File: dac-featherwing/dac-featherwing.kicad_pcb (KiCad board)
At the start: 2 copper layers, 22.9 x 50.7 mm, 14 parts, among them J1 BOT, J2 TOP, U1 WM1824

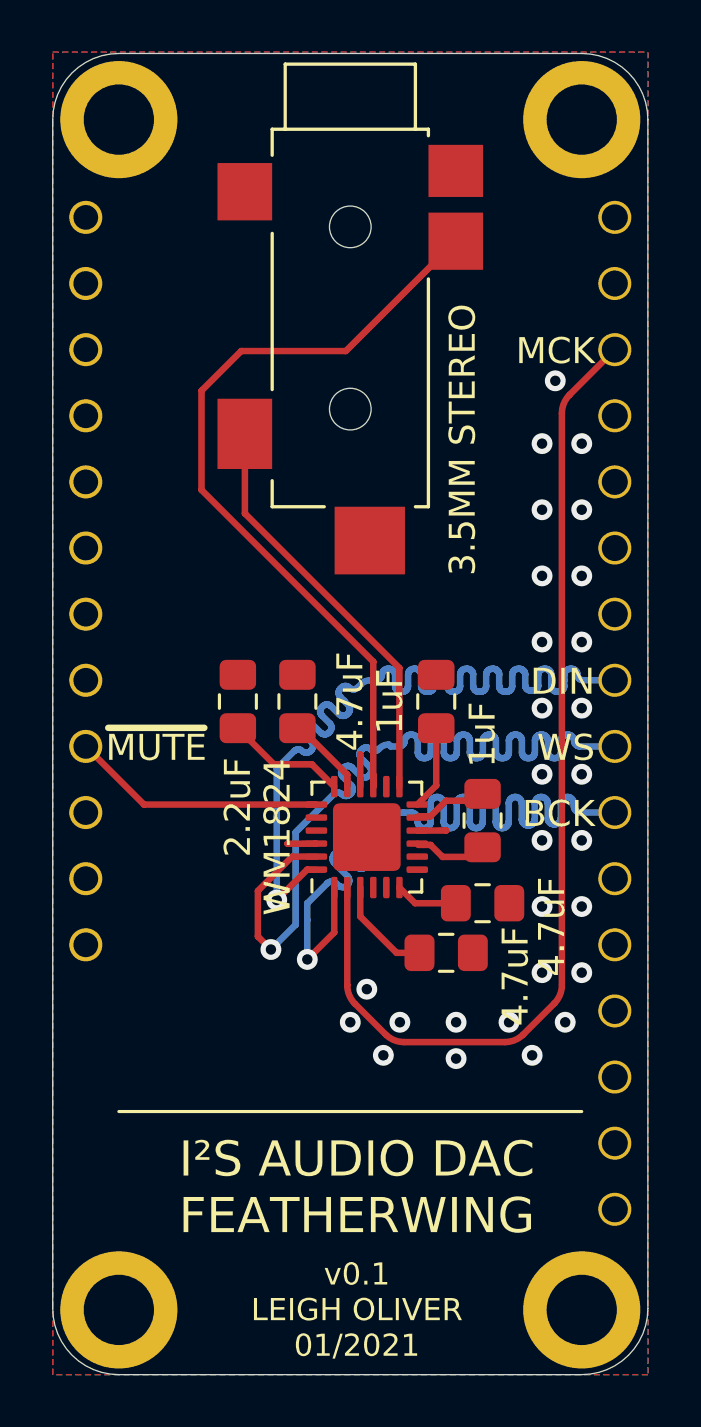
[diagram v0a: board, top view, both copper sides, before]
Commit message: Fixed no power routed to DAC
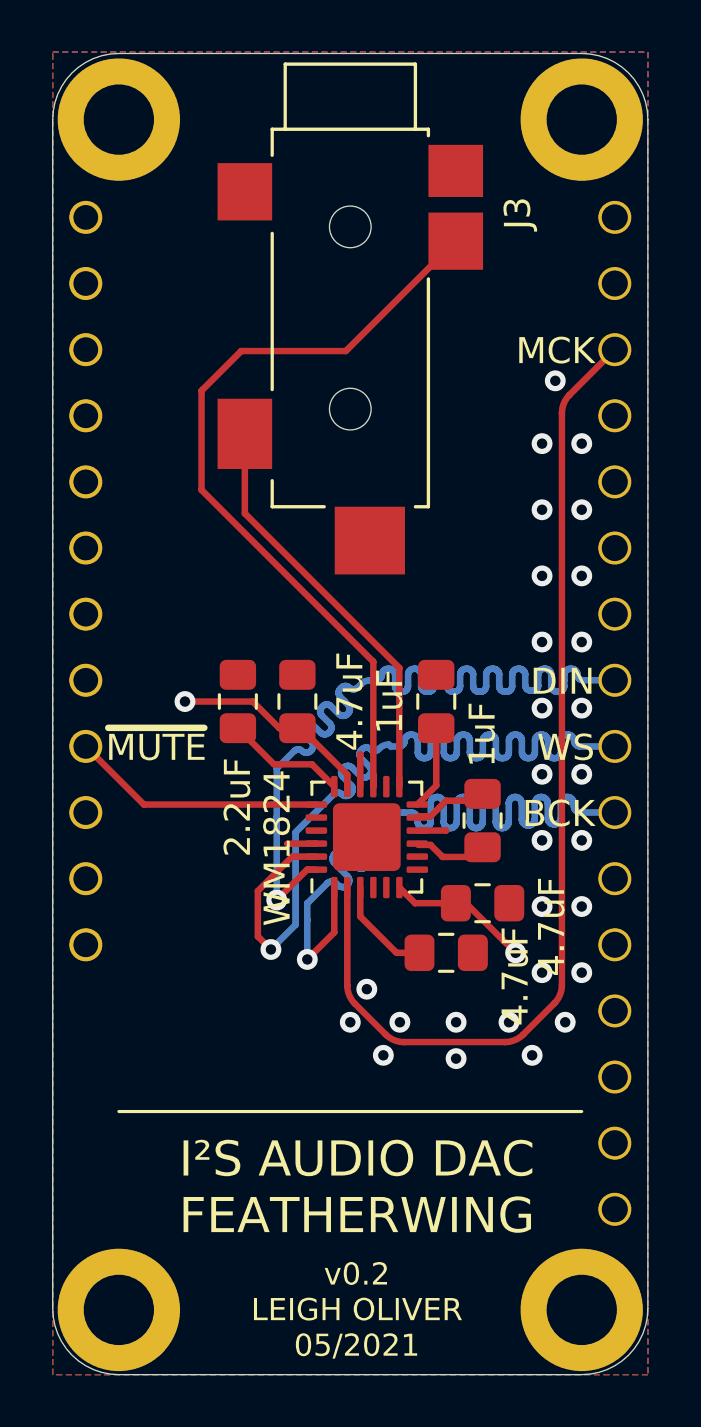
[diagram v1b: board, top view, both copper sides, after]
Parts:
- removed 3.5MM STEREO: 35RASMT4BHNTRX, Footprints:SWITCHCRAFT_35RASMT4BHNTRX
- removed ? (x3): , 
- removed the REF** at (157.5, 120.9)
- added J3: 35RASMT4BHNTRX, Footprints:SWITCHCRAFT_35RASMT4BHNTRX, F.Cu at (166.4, 82.8)
- added REF**: MountingHole_2.7mm_M2.5_DIN965_Pad, MountingHole:MountingHole_2.7mm_M2.5_DIN965_Pad, F.Cu at (157.5, 75.2)
- added REF**: MountingHole_2.7mm_M2.5_DIN965_Pad, MountingHole:MountingHole_2.7mm_M2.5_DIN965_Pad, F.Cu at (175.3, 120.9)
- added REF**: MountingHole_2.7mm_M2.5_DIN965_Pad, MountingHole:MountingHole_2.7mm_M2.5_DIN965_Pad, F.Cu at (157.5, 120.9)
- added REF**: MountingHole_2.7mm_M2.5_DIN965_Pad, MountingHole:MountingHole_2.7mm_M2.5_DIN965_Pad, F.Cu at (175.3, 75.2)
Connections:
- C2 pad 1: Net-(C2-Pad1) -> +3V3
- C5 pad 1: Net-(C5-Pad1) -> +3V3
- U1 pad 14: no_connect_43 -> unconnected-(U1-Pad14)
- U1 pad 17: Net-(C5-Pad1) -> +3V3
- U1 pad 2: /U1RXD/CLK_OUT3 -> unconnected-(U1-Pad2)
- U1 pad 20: no_connect_44 -> unconnected-(U1-Pad20)
- U1 pad 21: no_connect_46 -> unconnected-(U1-Pad21)
- U1 pad 4: no_connect_40 -> unconnected-(U1-Pad4)
- U1 pad 5: no_connect_41 -> unconnected-(U1-Pad5)
- U1 pad 6: Net-(C2-Pad1) -> +3V3
- U1 pad 7: no_connect_42 -> unconnected-(U1-Pad7)
- U1 pad 8: no_connect_45 -> unconnected-(U1-Pad8)
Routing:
- net unconnected-(U1-Pad2): track 0.00 -> 39.3 mm
- net /U1RXD/CLK_OUT3: track 39.3 -> 0.00 mm
- net +3V3: track 0.00 -> 13.4 mm, vias 0 -> 2
- net Net-(C5-Pad1): track 3.12 -> 0.00 mm
- net Net-(C2-Pad1): track 2.42 -> 0.00 mm
- added copper zone on B.Cu, net +3V3
- removed copper zone on B.Cu, net GND
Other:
- board text added: "v0.2 LEIGH OLIVER 05/2021"
- board text removed: "v0.1 LEIGH OLIVER 01/2021"
